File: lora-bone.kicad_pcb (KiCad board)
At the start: 2 copper layers, 30 x 100 mm, 30 parts, among them J1 Analog IN, J10 GS2, J11 GS2, J12 GS2, J13 GS2, J14 POWER OUT, J2 POWER, J3 Bluepill left, J4 PWM OUT, J5 SPI OUT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

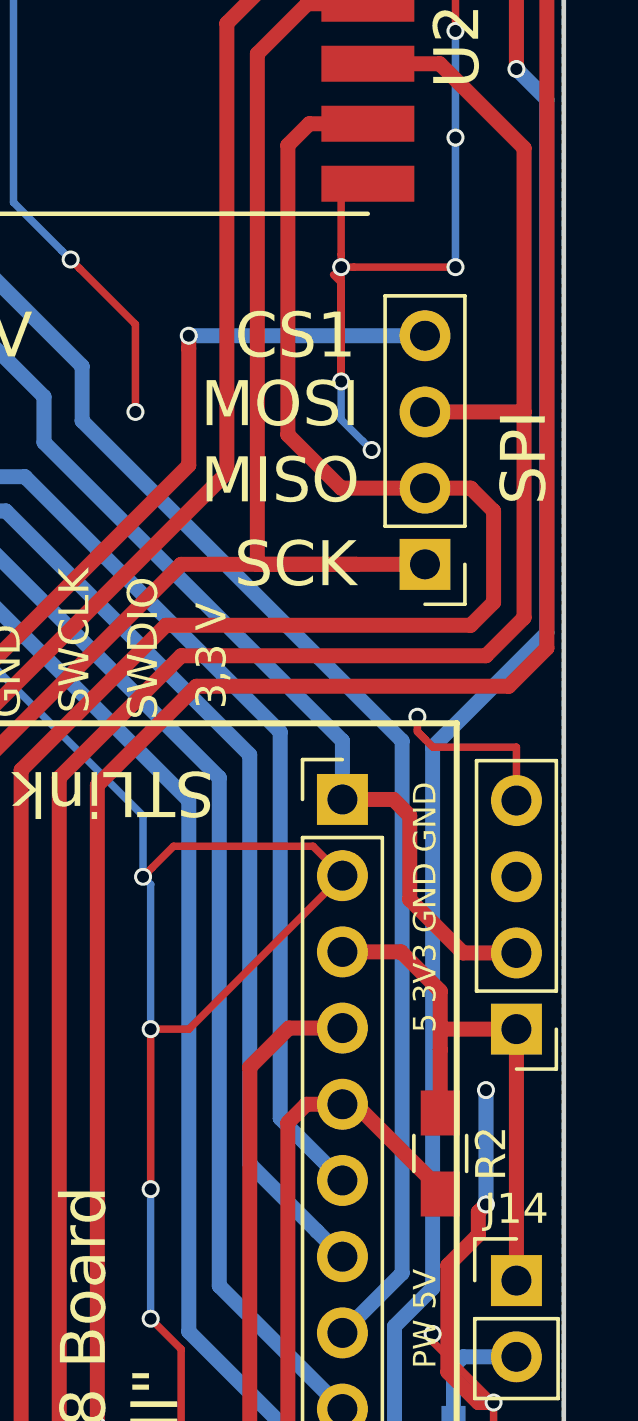
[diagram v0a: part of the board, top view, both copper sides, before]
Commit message: moved CCCAC Logo a bit, deactivated one reference
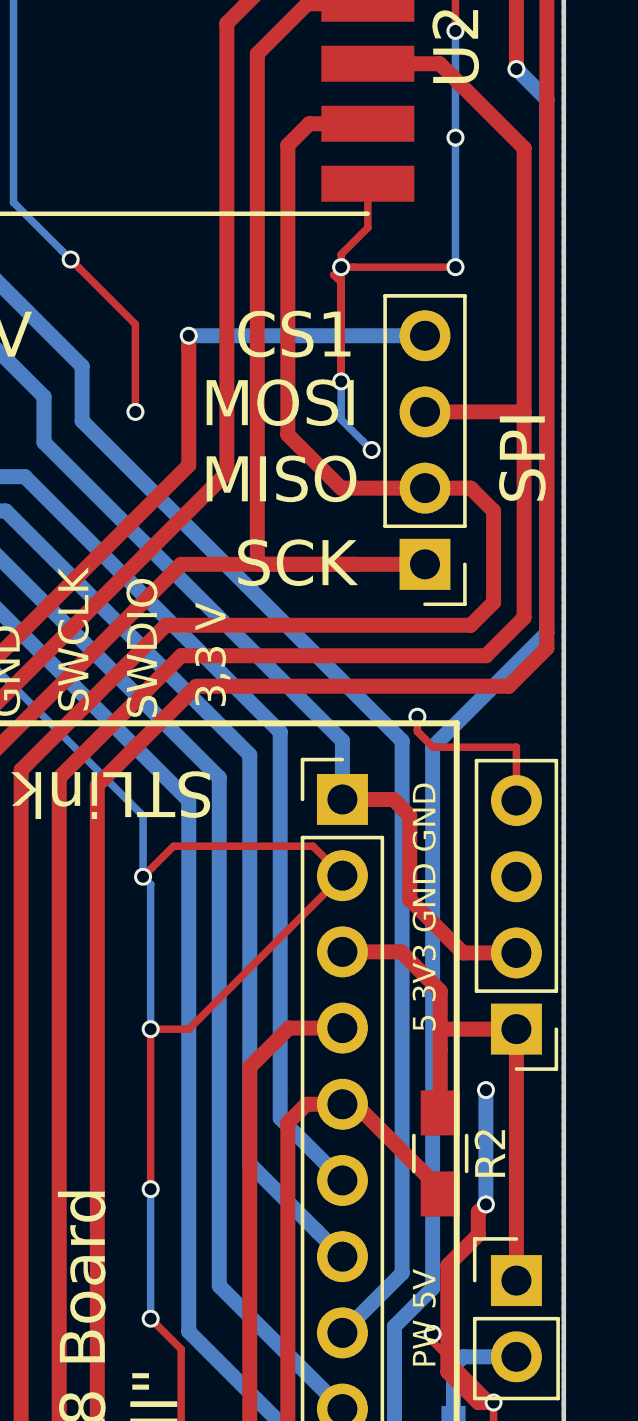
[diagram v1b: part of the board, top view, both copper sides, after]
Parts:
- moved G*** 2.29 mm to (43.6, 111.3)
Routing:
- net GND: track 403.6 -> 404.9 mm
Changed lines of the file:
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@@
     (thickness 1.6)
     (drawings 41)
-    (tracks 533)
+    (tracks 534)
     (zones 0)
     (modules 30)
@@
     (35 F.Paste user)
     (36 B.SilkS user)
-    (37 F.SilkS user hide)
+    (37 F.SilkS user)
     (38 B.Mask user)
     (39 F.Mask user)
@@
   )
   (setup
-    (last_trace_width 0.5)
+    (last_trace_width 0.25)
     (user_trace_width 0.5)
     (user_trace_width 1)
@@
   )
   (module LOGO (layer B.Cu)
-    (at 43.434 108.966 90)
+    (at 43.561 111.252 90)
     (fp_text reference G*** (at 0 0 90) (layer B.SilkS) hide
       (effects (font (thickness 0.3)) (justify mirror))
@@
     (descr "Through hole straight pin header, 1x02, 2.54mm pitch, single row")
     (tags "Through hole pin header THT 1x02 2.54mm single row")
-    (fp_text reference J14 (at 0 -2.39) (layer F.SilkS)
+    (fp_text reference J14 (at 0 -2.39) (layer F.SilkS) hide
       (effects (font (size 1 1) (thickness 0.15)))
     )
@@
   (segment (start 55.88 105.156) (end 55.88 105.84) (width 0.5) (layer F.Cu) (net 2))
   (segment (start 55.88 107.95) (end 55.88 105.84) (width 0.5) (layer F.Cu) (net 2))
+  (segment (start 52.466 76.976) (end 53.467 76.976) (width 0.25) (layer F.Cu) (net 3))
+  (segment (start 53.467 76.976) (end 53.467 78.44274) (width 0.25) (layer F.Cu) (net 3))
+  (segment (start 53.467 78.44274) (end 52.578004 79.331736) (width 0.25) (layer F.Cu) (net 3))
+  (segment (start 52.578004 79.331736) (end 52.578004 79.756) (width 0.25) (layer F.Cu) (net 3))
   (segment (start 45.72 81.661) (end 43.860999 79.801999) (width 0.25) (layer F.Cu) (net 3))
   (segment (start 45.72 84.582) (end 45.72 81.661) (width 0.25) (layer F.Cu) (net 3))
@@
   (segment (start 56.388 75.438) (end 56.388 79.756) (width 0.25) (layer B.Cu) (net 3))
   (via (at 56.388 79.756) (size 0.6) (drill 0.4) (layers F.Cu B.Cu) (net 3))
-  (segment (start 52.578004 77.088004) (end 52.578004 79.331736) (width 0.25) (layer F.Cu) (net 3))
-  (segment (start 52.466 76.976) (end 52.578004 77.088004) (width 0.25) (layer F.Cu) (net 3))
-  (segment (start 52.578004 79.331736) (end 52.578004 79.756) (width 0.25) (layer F.Cu) (net 3))
   (via (at 52.578004 79.756) (size 0.6) (drill 0.4) (layers F.Cu B.Cu) (net 3))
   (segment (start 56.388 71.882002) (end 56.388002 71.882) (width 0.25) (layer B.Cu) (net 3))

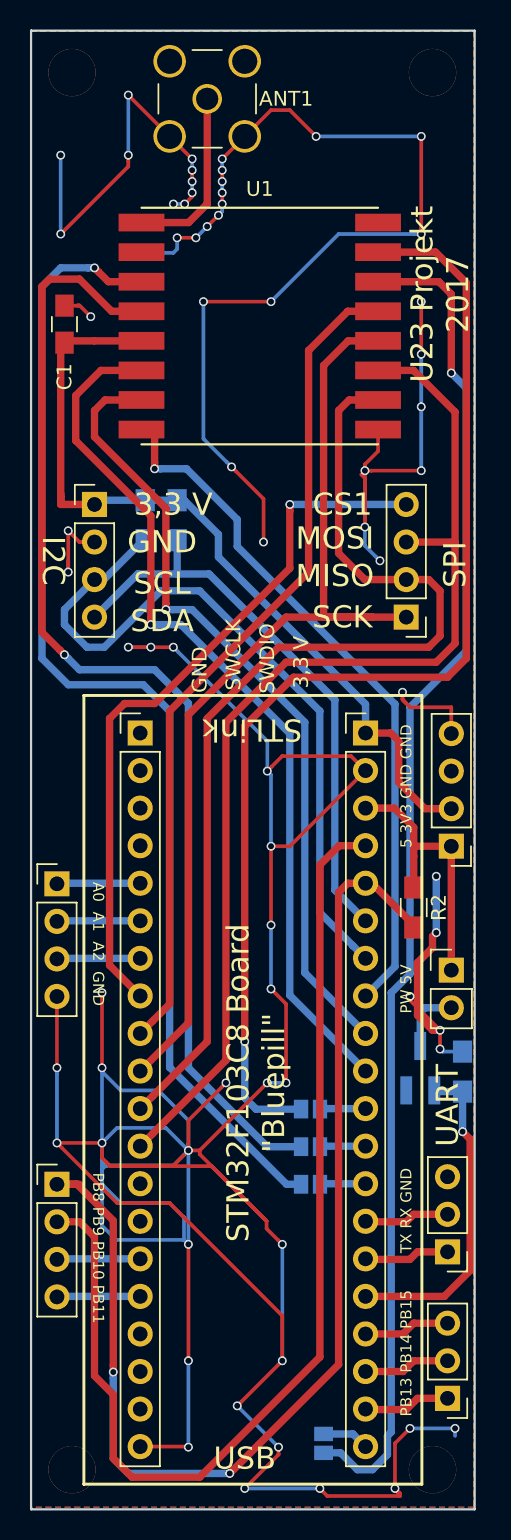
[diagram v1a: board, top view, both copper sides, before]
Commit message: Make the Board 2 mm shorter
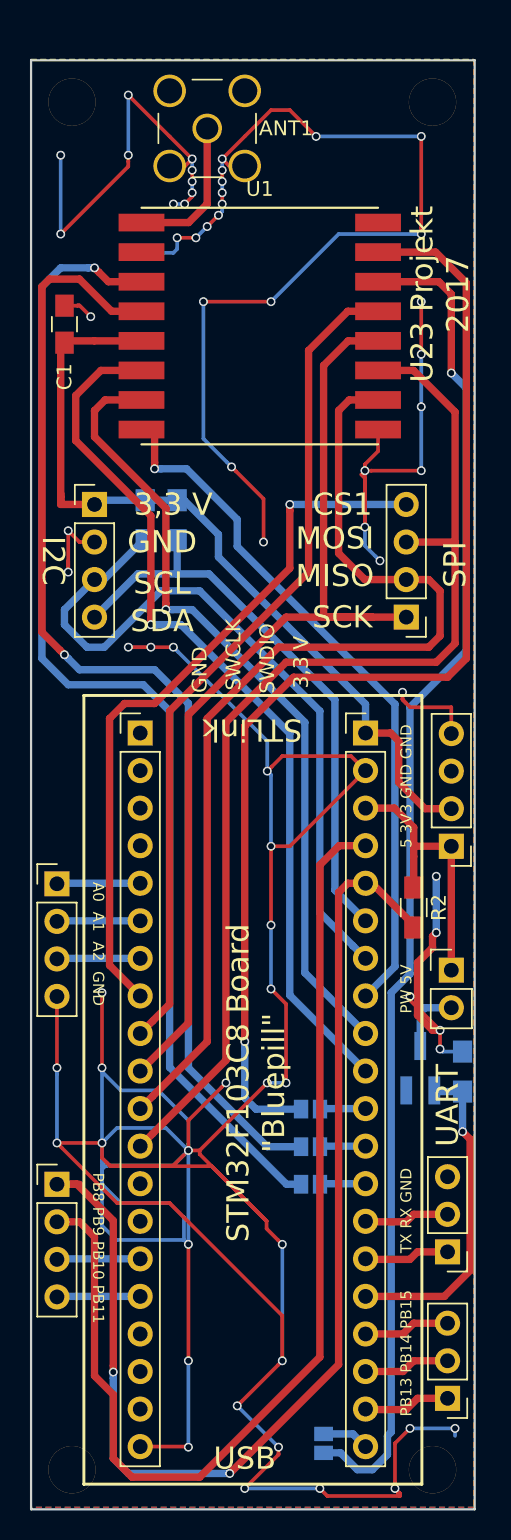
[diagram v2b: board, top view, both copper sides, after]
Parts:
- moved G*** 3.42 mm to (46.5, 70.6)
- moved ANT1 2.00 mm to (41.9, 56.6)
- moved REF** 2.00 mm to (32.8, 54.8)
- moved REF** 2.00 mm to (57.1, 54.8)
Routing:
- net GND: track 404.9 -> 408.4 mm
- net Net-(ANT1-Pad1): track 11.1 -> 9.04 mm
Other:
- board size 30 x 100 mm -> 30 x 98 mm
